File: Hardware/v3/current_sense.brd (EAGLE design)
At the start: 70.1 x 59.9 mm, 38 parts, among them J1 SCREW-TERMINAL_2_0.100, J2 SCREW-TERMINAL_2_0.100, J3 SCREW-TERMINAL_2_0.100, J4 SCREW-TERMINAL_2_0.100, U1 MAX9923H, U2 LP3985

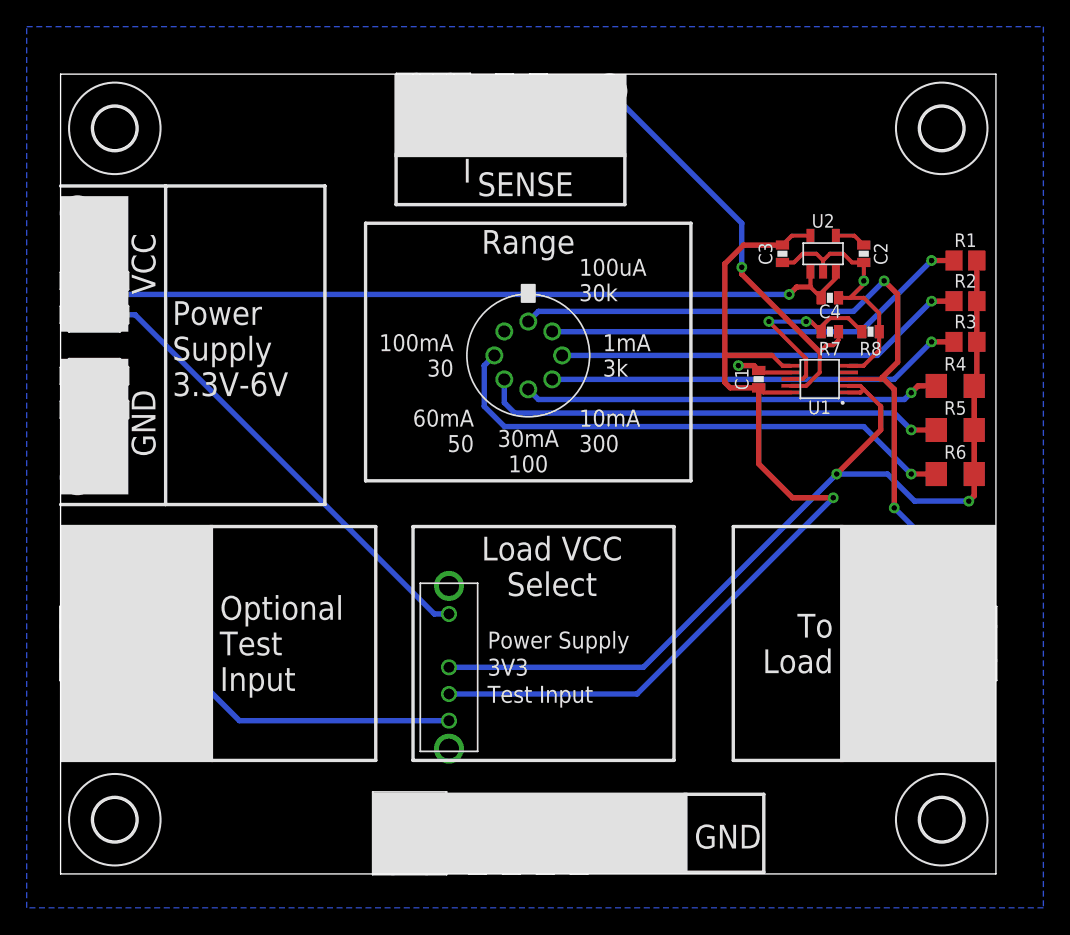
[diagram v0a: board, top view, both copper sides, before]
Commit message: better silkscreen
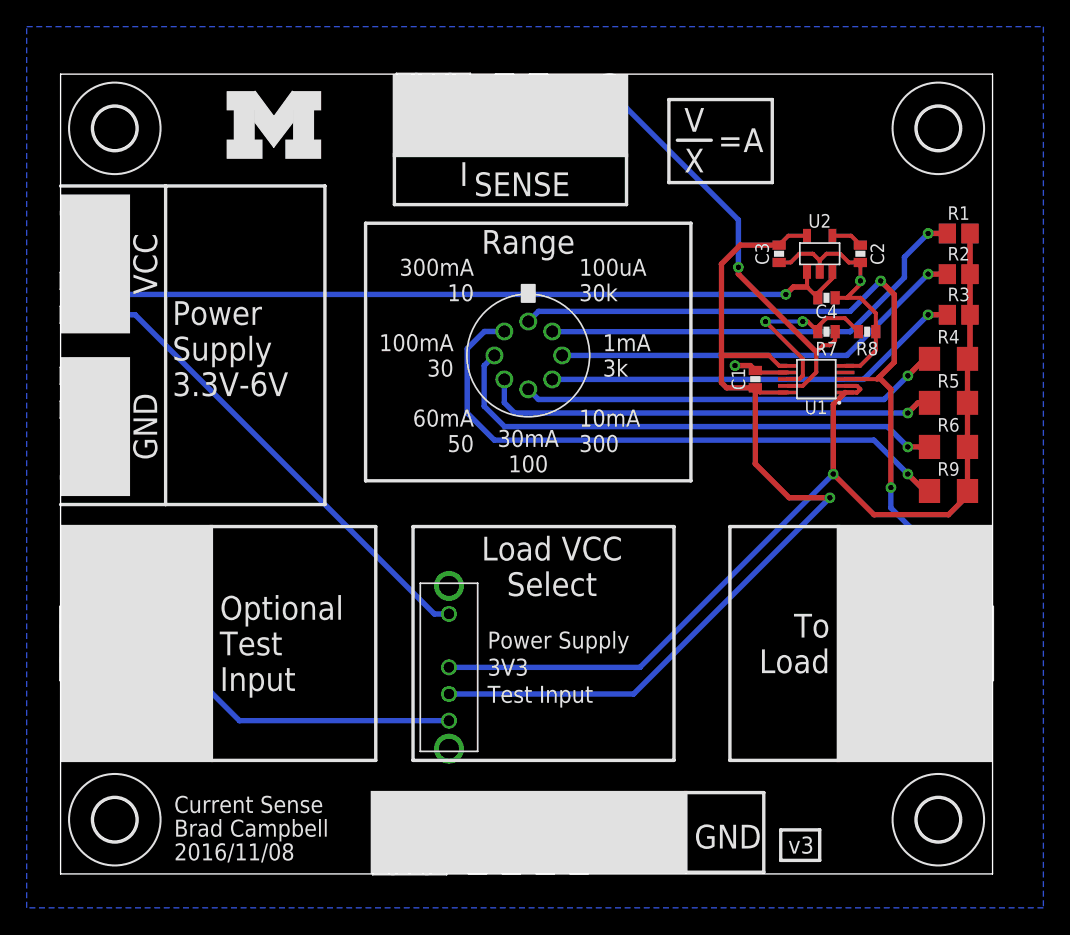
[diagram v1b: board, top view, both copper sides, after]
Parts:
- added LOGO2: UMICH_SOLID_MEDIUM, logos:UMICH_SOLID_200MIL
- added R9: 0.04, resistor:R1206
- S1: value RM106772BCB -> RM100772BCB
- moved R1 2.09 mm to (67.3, 48.0)
- moved R2 2.09 mm to (67.3, 45.0)
- moved R3 2.09 mm to (67.3, 41.9)
- moved R4 2.09 mm to (66.5, 38.6)
- moved R5 2.09 mm to (66.5, 35.3)
- moved R6 2.09 mm to (66.5, 32.0)
- moved H2 0.25 mm to (65.8, 4.06)
- moved H3 0.25 mm to (65.8, 55.9)
- moved R8 0.25 mm to (60.5, 40.6)
- moved TP1 0.25 mm to (3.05, 10.9)
- moved TP2 0.25 mm to (3.05, 23.6)
- moved C1 0.25 mm to (52.1, 37.1)
- moved C2 0.25 mm to (59.9, 46.5)
- moved C3 0.25 mm to (53.8, 46.5)
- moved C4 0.25 mm to (57.4, 43.2)
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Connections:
- new net N$9: R9.1, S1.7
- net VIN: now also R9.2
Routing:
- net N$9: track 0.00 -> 45.2 mm, vias 0 -> 1
- net N$6: track 40.1 -> 38.8 mm
- net N$1: track 32.3 -> 33.6 mm
- net N$5: track 35.0 -> 34.3 mm
- net VIN: track 74.8 -> 75.4 mm, vias 2 -> 1
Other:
- board size 70.1 x 59.9 mm -> 69.8 x 59.9 mm
- board text added: "2016/11/08"
- board text added: "300mA 10"
- board text added: "="
- board text added: "A"
- board text added: "Brad Campbell"
- board text added: "Current Sense"
- board text added: "V"
- board text added: "X"
- board text added: "v3"

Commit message: renumbered parts and added bom
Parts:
- C1: value 0.1uF -> 0.01uF
- C2: value 0.01uF -> 0.1uF
- R1: value 120 -> 0.04; device resistor:R0805 -> resistor:R1206
- R2: value 12 -> 0.12; device resistor:R0805 -> resistor:R1206
- R3: value 1.2 -> 0.2; device resistor:R0805 -> resistor:R1206
- R5: value 0.2 -> 1.2; device resistor:R1206 -> resistor:R0805
- R6: value 0.12 -> 12; device resistor:R1206 -> resistor:R0805
- R7: value 249k -> 120; device passives:0603-RES -> resistor:R0805
- R9: value 0.04 -> 249k; device resistor:R1206 -> passives:0603-RES
- TP7: value TEST_POINT_0.112IN -> TEST_POINT_0.040IN; device headers:TESTPOINT_0.112IN -> headers:TESTPOINT_0.040IN
- TP8: value TEST_POINT_0.040IN -> TEST_POINT_0.112IN; device headers:TESTPOINT_0.040IN -> headers:TESTPOINT_0.112IN
- moved TP7 56.0 mm to (41.1, 58.7)
- moved TP8 56.0 mm to (44.5, 2.79)
- moved R1 19.3 mm to (66.5, 28.7)
- moved R9 15.0 mm to (57.4, 40.6)
- moved R2 13.0 mm to (66.5, 32.0)
- moved R6 13.0 mm to (67.3, 45.0)
- moved R7 12.3 mm to (67.3, 48.0)
- moved C1 12.3 mm to (59.9, 46.5), turned to 270 degrees
- moved C2 12.3 mm to (52.1, 37.1), turned to 90 degrees
- moved R3 6.65 mm to (66.5, 35.3)
- moved R5 6.65 mm to (67.3, 41.9)
- renumbered JP1 to J5, JP2 to J7, JP3 to J8, JP4 to J6, JP5 to J10, JP6 to J9, S3 to S2
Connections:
- net GND: now also TP8.1; no longer TP7.1
- net N$1: now also R7.1; no longer R1.1
- net N$2: now also R6.1; no longer R2.1
- net N$3: now also R5.1; no longer R3.1
- net N$5: now also R3.1; no longer R5.1
- net N$6: now also R2.1; no longer R6.1
- net N$7: now also R9.1; no longer R7.1
- net N$8: now also C1.1; no longer C2.1
- net N$9: now also R1.1; no longer R9.1
- net VCC: now also C2.1; no longer C1.1
- net VIN: now also R7.2; no longer R9.2
- net VOUT: now also R9.2, TP7.TESTPOINT; no longer R7.2, TP8.TESTPOINT

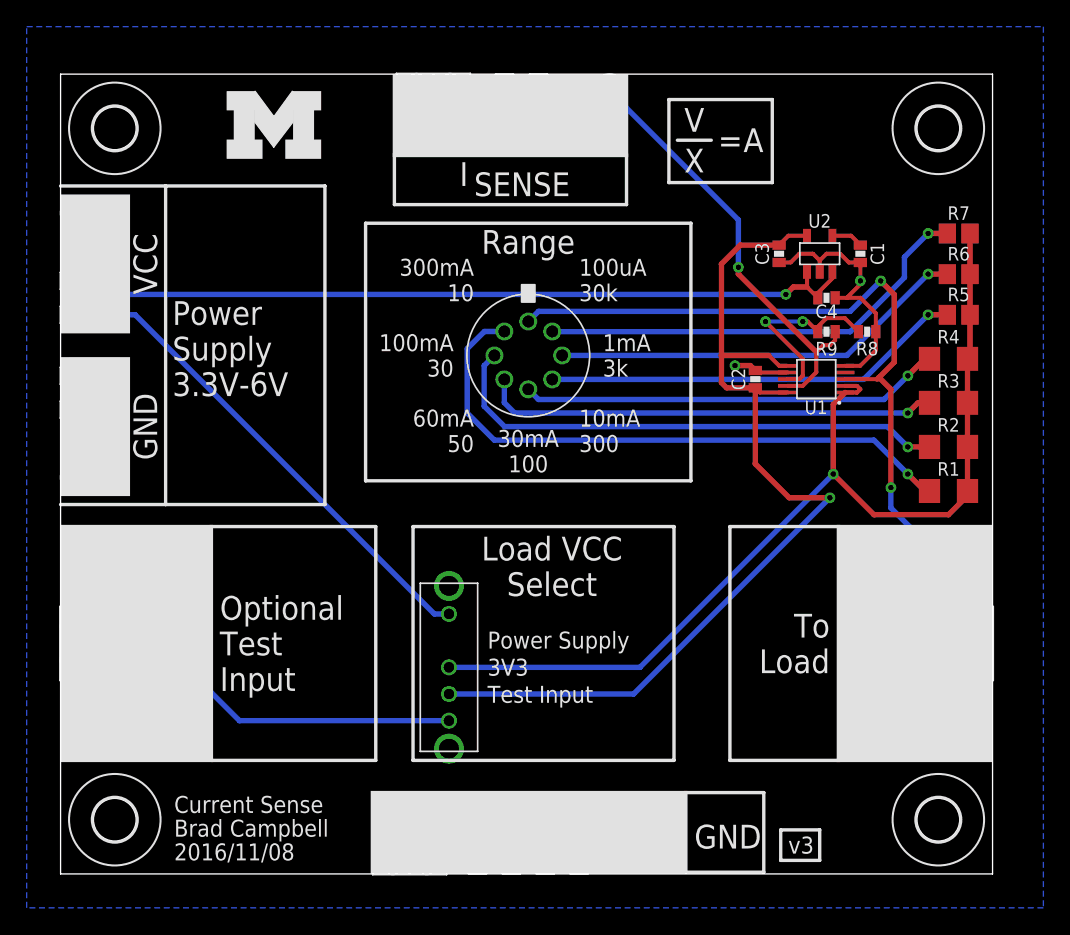
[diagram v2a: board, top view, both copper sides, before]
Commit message: updated current sense and zips
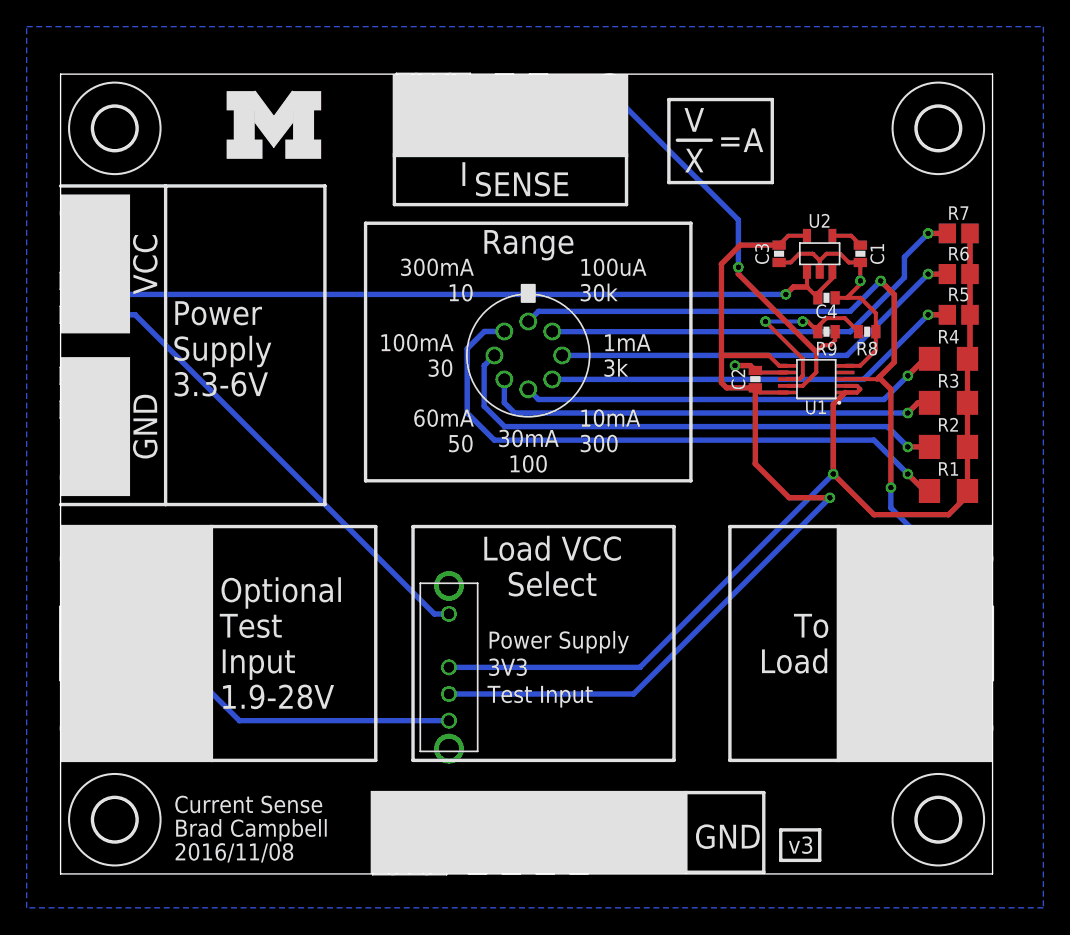
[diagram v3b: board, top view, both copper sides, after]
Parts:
- moved TP1 1.78 mm to (1.27, 10.9)
- moved TP2 1.78 mm to (1.27, 23.6)
- moved TP5 1.78 mm to (68.6, 23.6)
- moved TP6 1.78 mm to (68.6, 10.9)
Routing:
- net RS-: track 82.1 -> 85.4 mm
- net LOAD_IN: track 49.0 -> 50.5 mm
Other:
- board text added: "Optional Test Input 1.9-28V"
- board text added: "Power Supply 3.3-6V"
- board text removed: "Optional Test Input"
- board text removed: "Power Supply 3.3V-6V"
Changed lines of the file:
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@@
 <text x="8.382" y="39.37" size="1.778" layer="21" font="vector" ratio="12" align="center-left">Power
 Supply
-3.3V-6V</text>
+3.3-6V</text>
 <wire x1="7.874" y1="27.686" x2="19.812" y2="27.686" width="0.254" layer="21"/>
 <wire x1="19.812" y1="27.686" x2="19.812" y2="51.562" width="0.254" layer="21"/>
@@
 <text x="11.938" y="17.272" size="1.778" layer="21" font="vector" ratio="12" align="center-left">Optional
 Test
-Input</text>
+Input
+1.9-28V</text>
 <text x="38.862" y="42.926" size="1.27" layer="21" font="vector" ratio="12">100uA
 30k</text>
@@
 </class>
 </classes>
-<designrules name="sunstone-2lyr_v1.0.0.3">
+<designrules name="sunstone-2lyr_v1.0.0.3 *">
 <description language="en">&lt;b&gt;EAGLE Design Rules for *2* Layer Designs (DS)&lt;/b&gt;
 &lt;p&gt;
@@
 <param name="srMinRoundness" value="0mil"/>
 <param name="srMaxRoundness" value="0mil"/>
-<param name="slThermalIsolate" value="10mil"/>
+<param name="slThermalIsolate" value="25mil"/>
 <param name="slThermalsForVias" value="0"/>
 <param name="dpMaxLengthDifference" value="10mm"/>
@@
 <elements>
 <element name="U1" library="chips" package="UMAX10" value="MAX9923H" x="56.642" y="37.084" smashed="yes" rot="R90">
-<attribute name="DIGIKEY" value="MAX9923HEUB+-ND" x="71.882" y="70.104" size="1.778" layer="27" rot="R90" display="off"/>
+<attribute name="DIGIKEY" value="MAX9922EUB+TCT-ND" x="71.882" y="70.104" size="1.778" layer="27" rot="R90" display="off"/>
 <attribute name="NAME" x="56.622" y="35.474" size="1.016" layer="21" font="vector" ratio="12" rot="R180" align="bottom-center"/>
 </element>
@@
 <attribute name="DIGIKEY" value="277-1273-ND" x="3.048" y="17.272" size="1.778" layer="27" rot="R270" display="off"/>
 </element>
-<element name="TP1" library="headers" package="TESTPOINT_0.040IN" value="TEST_POINT_0.040IN" x="3.048" y="10.922" smashed="yes">
-<attribute name="DIGIKEY" value="5001K-ND" x="3.048" y="10.922" size="1.778" layer="27" display="off"/>
-<attribute name="VALUE" x="3.048" y="8.382" size="1.016" layer="27" font="vector" ratio="12" align="bottom-center"/>
-</element>
-<element name="TP2" library="headers" package="TESTPOINT_0.040IN" value="TEST_POINT_0.040IN" x="3.048" y="23.622" smashed="yes">
-<attribute name="DIGIKEY" value="5001K-ND" x="3.048" y="23.622" size="1.778" layer="27" display="off"/>
-<attribute name="VALUE" x="3.048" y="21.082" size="1.016" layer="27" font="vector" ratio="12" align="bottom-center"/>
+<element name="TP1" library="headers" package="TESTPOINT_0.040IN" value="TEST_POINT_0.040IN" x="1.27" y="10.922" smashed="yes">
+<attribute name="DIGIKEY" value="5001K-ND" x="1.27" y="10.922" size="1.778" layer="27" display="off"/>
+<attribute name="VALUE" x="1.27" y="8.382" size="1.016" layer="27" font="vector" ratio="12" align="bottom-center"/>
+</element>
+<element name="TP2" library="headers" package="TESTPOINT_0.040IN" value="TEST_POINT_0.040IN" x="1.27" y="23.622" smashed="yes">
+<attribute name="DIGIKEY" value="5001K-ND" x="1.27" y="23.622" size="1.778" layer="27" display="off"/>
+<attribute name="VALUE" x="1.27" y="21.082" size="1.016" layer="27" font="vector" ratio="12" align="bottom-center"/>
 </element>
 <element name="J5" library="pinhead" package="1X02" value="" x="8.89" y="17.272" smashed="yes" rot="R90">
@@
 <attribute name="VALUE" x="57.531" y="19.812" size="1.27" layer="27" rot="R270"/>
 </element>
-<element name="TP5" library="headers" package="TESTPOINT_0.040IN" value="TEST_POINT_0.040IN" x="66.802" y="23.622" smashed="yes" rot="R180">
-<attribute name="DIGIKEY" value="5001K-ND" x="66.802" y="23.622" size="1.778" layer="27" font="vector" ratio="12" rot="R180" display="off"/>
-<attribute name="VALUE" x="66.802" y="26.162" size="1.016" layer="27" font="vector" ratio="12" rot="R180" align="bottom-center"/>
-</element>
-<element name="TP6" library="headers" package="TESTPOINT_0.040IN" value="TEST_POINT_0.040IN" x="66.802" y="10.922" smashed="yes" rot="R180">
-<attribute name="DIGIKEY" value="5001K-ND" x="66.802" y="10.922" size="1.778" layer="27" font="vector" ratio="12" rot="R180" display="off"/>
-<attribute name="VALUE" x="66.802" y="13.462" size="1.016" layer="27" font="vector" ratio="12" rot="R180" align="bottom-center"/>
+<element name="TP5" library="headers" package="TESTPOINT_0.040IN" value="TEST_POINT_0.040IN" x="68.58" y="23.622" smashed="yes" rot="R180">
+<attribute name="DIGIKEY" value="5001K-ND" x="68.58" y="23.622" size="1.778" layer="27" font="vector" ratio="12" rot="R180" display="off"/>
+<attribute name="VALUE" x="68.58" y="26.162" size="1.016" layer="27" font="vector" ratio="12" rot="R180" align="bottom-center"/>
+</element>
+<element name="TP6" library="headers" package="TESTPOINT_0.040IN" value="TEST_POINT_0.040IN" x="68.58" y="10.922" smashed="yes" rot="R180">
+<attribute name="DIGIKEY" value="5001K-ND" x="68.58" y="10.922" size="1.778" layer="27" font="vector" ratio="12" rot="R180" display="off"/>
+<attribute name="VALUE" x="68.58" y="13.462" size="1.016" layer="27" font="vector" ratio="12" rot="R180" align="bottom-center"/>
 </element>
 <element name="J3" library="headers" package="CONN_BLOCK_2" value="SCREW-TERMINAL_2_0.100" x="26.162" y="3.048" smashed="yes">
@@
 <wire x1="61.341" y1="37.211" x2="61.214" y2="37.084" width="0.4064" layer="1"/>
 <wire x1="61.214" y1="37.084" x2="58.812" y2="37.084" width="0.3048" layer="1"/>
-<wire x1="66.802" y1="23.622" x2="66.802" y2="18.542" width="0.4064" layer="16"/>
 <wire x1="66.802" y1="16.002" x2="66.802" y2="18.542" width="0.4064" layer="16"/>
-<wire x1="66.802" y1="10.922" x2="66.802" y2="16.002" width="0.4064" layer="16"/>
 <wire x1="60.706" y1="18.542" x2="66.802" y2="18.542" width="0.4064" layer="16"/>
 <wire x1="60.706" y1="16.002" x2="60.706" y2="18.542" width="0.4064" layer="16"/>
 <wire x1="66.802" y1="16.002" x2="60.706" y2="16.002" width="0.4064" layer="16"/>
-<wire x1="66.802" y1="23.622" x2="66.04" y2="23.622" width="0.4064" layer="16"/>
+<wire x1="68.58" y1="23.622" x2="66.04" y2="23.622" width="0.4064" layer="16"/>
 <via x="62.23" y="28.956" extent="1-16" drill="0.4064"/>
 <wire x1="62.23" y1="28.956" x2="62.23" y2="36.322" width="0.4064" layer="1"/>
@@
 <wire x1="62.23" y1="27.432" x2="62.23" y2="28.956" width="0.4064" layer="16"/>
 <wire x1="35.814" y1="42.164" x2="35.052" y2="41.402" width="0.4064" layer="16"/>
+<wire x1="68.58" y1="23.622" x2="68.58" y2="20.32" width="0.4064" layer="16"/>
+<wire x1="68.58" y1="20.32" x2="66.802" y2="18.542" width="0.4064" layer="16"/>
+<wire x1="68.58" y1="10.922" x2="68.58" y2="14.224" width="0.4064" layer="16"/>
+<wire x1="68.58" y1="14.224" x2="66.802" y2="16.002" width="0.4064" layer="16"/>
 </signal>
 <signal name="VOUT">
@@
 <contactref element="J5" pad="1"/>
 <contactref element="J5" pad="2"/>
-<wire x1="3.048" y1="10.922" x2="3.048" y2="16.002" width="0.4064" layer="16"/>
 <wire x1="3.048" y1="18.542" x2="3.048" y2="16.002" width="0.4064" layer="16"/>
-<wire x1="3.048" y1="23.622" x2="3.048" y2="18.542" width="0.4064" layer="16"/>
 <wire x1="8.89" y1="18.542" x2="3.048" y2="18.542" width="0.4064" layer="16"/>
 <wire x1="8.89" y1="16.002" x2="3.048" y2="16.002" width="0.4064" layer="16"/>
@@
 <wire x1="29.11" y1="11.486" x2="13.406" y2="11.486" width="0.4064" layer="16"/>
 <wire x1="13.406" y1="11.486" x2="8.89" y2="16.002" width="0.4064" layer="16"/>
+<wire x1="1.27" y1="10.922" x2="1.27" y2="14.224" width="0.4064" layer="16"/>
+<wire x1="1.27" y1="14.224" x2="3.048" y2="16.002" width="0.4064" layer="16"/>
+<wire x1="1.27" y1="23.622" x2="1.27" y2="20.32" width="0.4064" layer="16"/>
+<wire x1="1.27" y1="20.32" x2="3.048" y2="18.542" width="0.4064" layer="16"/>
 </signal>
 <signal name="N$9">
